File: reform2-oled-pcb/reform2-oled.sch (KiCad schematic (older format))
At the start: 14 parts, among them J1 AUX, U1 SSD1306

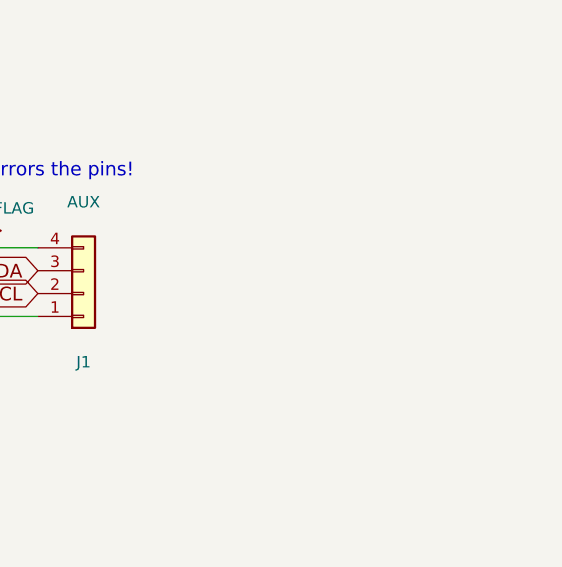
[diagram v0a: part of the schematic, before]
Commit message: WIP OLED now CERN-OHL-S 2.0
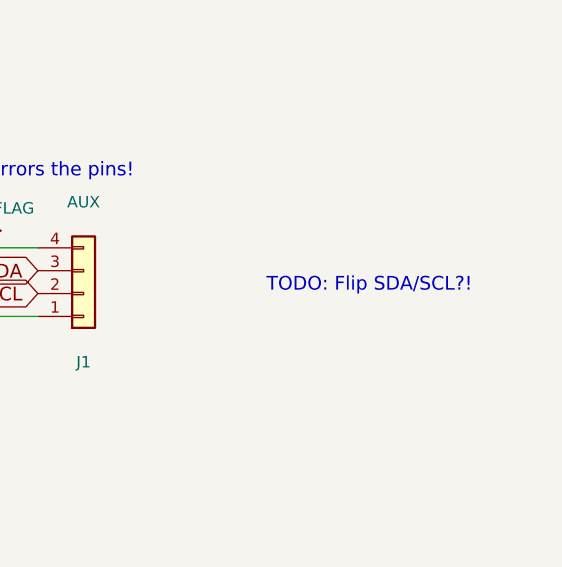
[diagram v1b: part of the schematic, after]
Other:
- note added: "TODO: Flip SDA/SCL?!"
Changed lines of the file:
@@
 EESchema Schematic File Version 4
-LIBS:reform2-oled-cache
-EELAYER 29 0
+EELAYER 30 0
 EELAYER END
 $Descr A4 11693 8268
 encoding utf-8
 Sheet 1 1
-Title "Reform Status Display OLED"
-Date "2019-11-07"
-Rev "D-1"
+Title "MNT Reform 2 Keyboard OLED"
+Date "2020-04-12"
+Rev "2.0D-4"
 Comp "MNT Research GmbH"
-Comment1 "License: GPLv3+"
-Comment2 "https://mntre.com"
-Comment3 ""
+Comment1 "https://mntre.com"
+Comment2 "Engineer: Lukas F. Hartmann"
+Comment3 "License: CERN-OHL-S 2.0"
 Comment4 ""
 $EndDescr
@@
 Wire Wire Line
 	2200 3650 2200 4250
+Text Notes 6650 3500 0    60   ~ 0
+TODO: Flip SDA/SCL?!
 $EndSCHEMATC

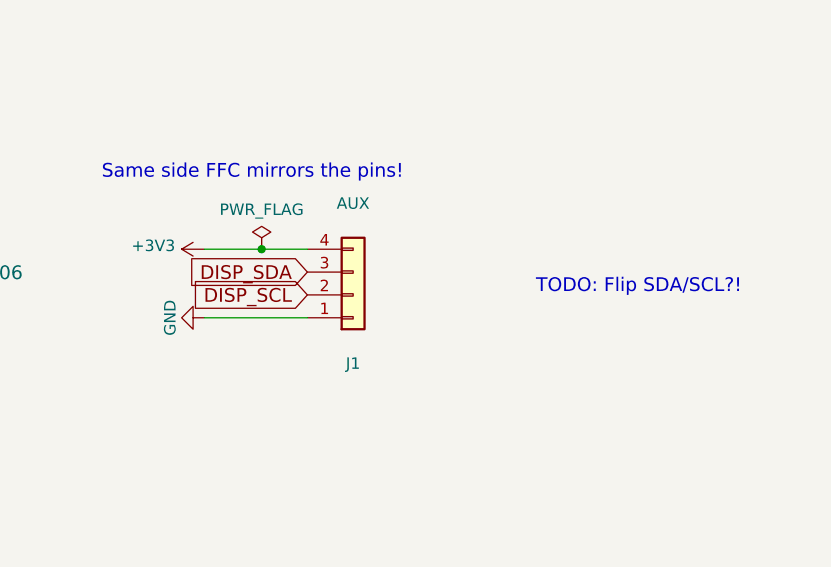
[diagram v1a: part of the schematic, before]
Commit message: reform2-oled: fix: swap sda/scl
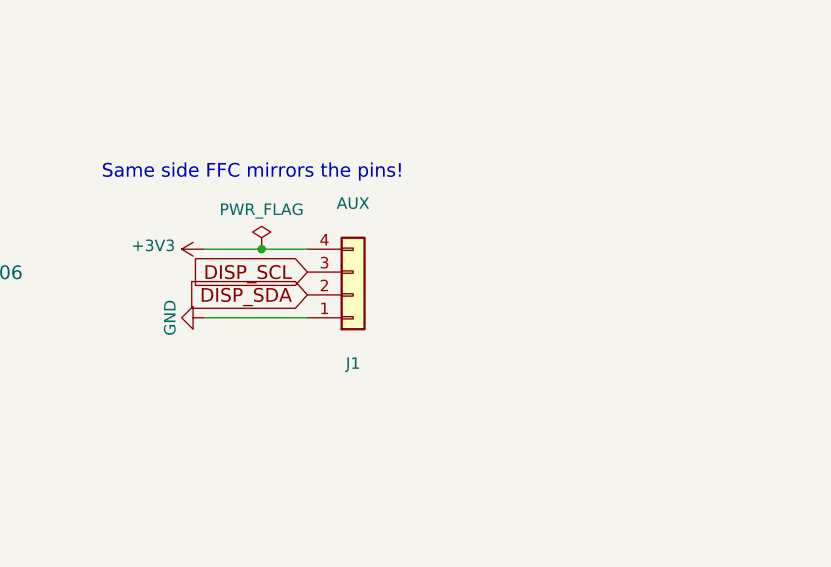
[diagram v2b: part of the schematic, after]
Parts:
- U1: Manufacturer (none) -> Enrich Electronics; Manufacturer_No (none) -> ENH-OB00910003
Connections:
- net DISP_SCL: now also J1.3 (Pin_3); no longer J1.2 (Pin_2)
- net DISP_SDA: now also J1.2 (Pin_2); no longer J1.3 (Pin_3)
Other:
- note removed: "TODO: Flip SDA/SCL?!"
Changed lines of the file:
@@
 Sheet 1 1
 Title "MNT Reform 2 Keyboard OLED"
-Date "2020-04-12"
+Date "2020-04-19"
 Rev "2.0D-4"
 Comp "MNT Research GmbH"
@@
 Text GLabel 3350 4050 0    60   Input ~ 0
 DISP_SDA
+Text GLabel 5650 3400 0    60   Input ~ 0
+DISP_SCL
 Text GLabel 5650 3500 0    60   Input ~ 0
-DISP_SCL
-Text GLabel 5650 3400 0    60   Input ~ 0
 DISP_SDA
 $Comp
@@
 F 2 "KiCad-SSD1306_OLED-0:SSD1306_OLED-0.91-128x32" H 3350 3350 60  0001 C CNN
 F 3 "" H 3350 3350 60  0001 C CNN
+F 4 "Enrich Electronics" H 3350 3350 50  0001 C CNN "Manufacturer"
+F 5 "ENH-OB00910003" H 3350 3350 50  0001 C CNN "Manufacturer_No"
 	1    3350 3350
 	0    1    1    0
@@
 Wire Wire Line
 	2200 3650 2200 4250
-Text Notes 6650 3500 0    60   ~ 0
-TODO: Flip SDA/SCL?!
 $EndSCHEMATC
